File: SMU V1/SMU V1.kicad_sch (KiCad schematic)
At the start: 0 parts

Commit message: i forget what i changed
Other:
- sheet GPS ports: added GPS_LDO_EN; removed PP3300_GPS_VBCKUP
- sheet IMU ports: added IMU_INT1, IMU_INT2, IMU_SPI, PP5000_IMU_VSUPP; removed none
- sheet Main IO ports: added CAN, VBATT+; removed none
- sheet Microcontroller ports: added CAN, GPS_UART, IMU_SPI; removed none
- sheet Power ports: added PP3300_LDO_VOUT, PP5000_BUCK_VOUT, PPVAR_VBATT_RAW; removed none

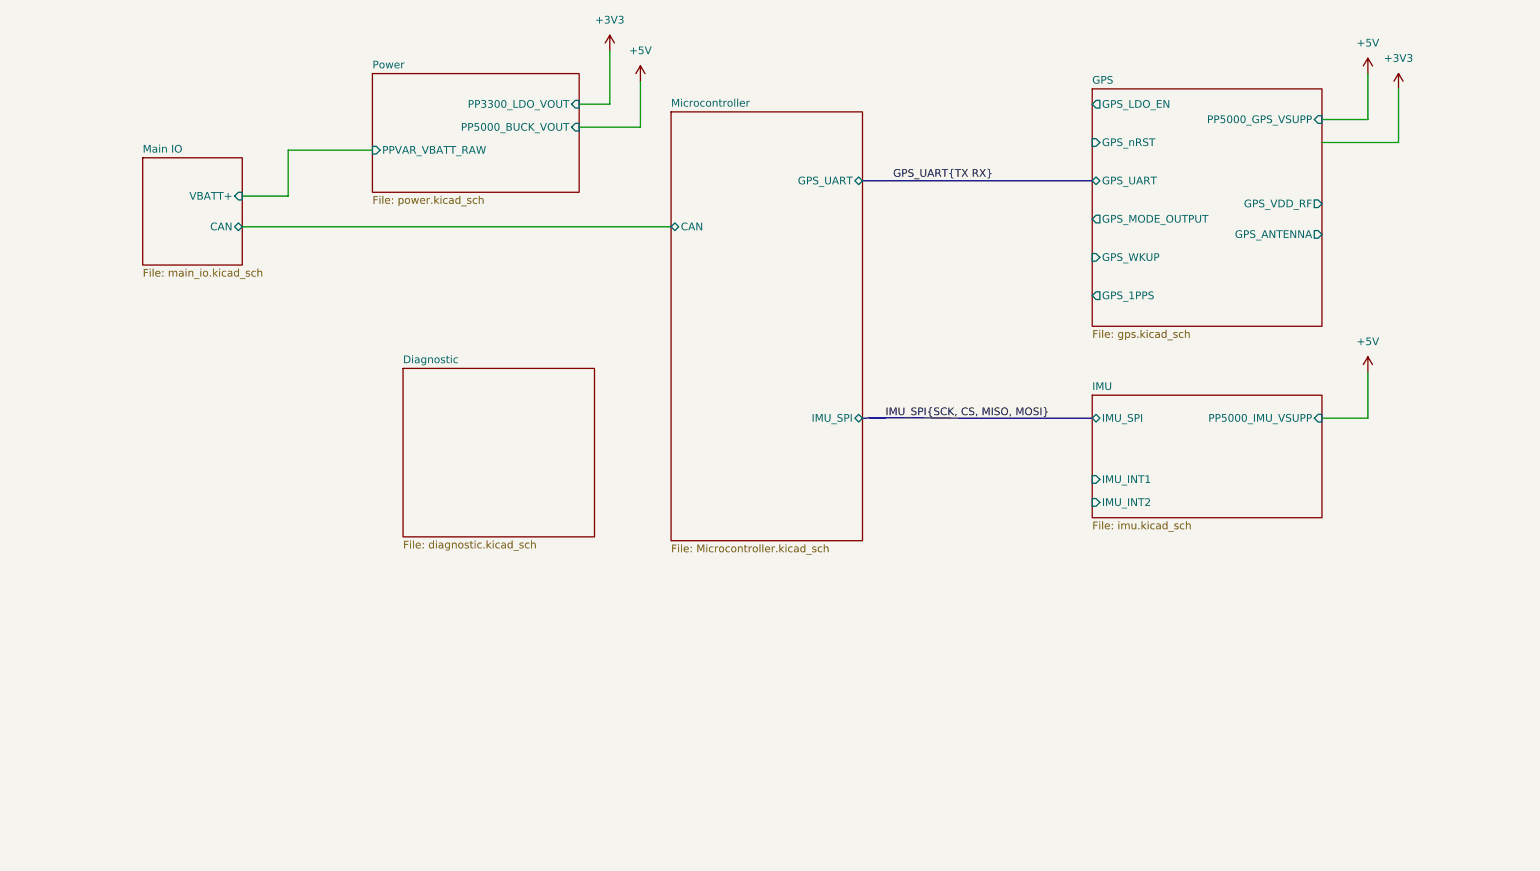
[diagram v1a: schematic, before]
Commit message: halfway done with routing, still needs antenna
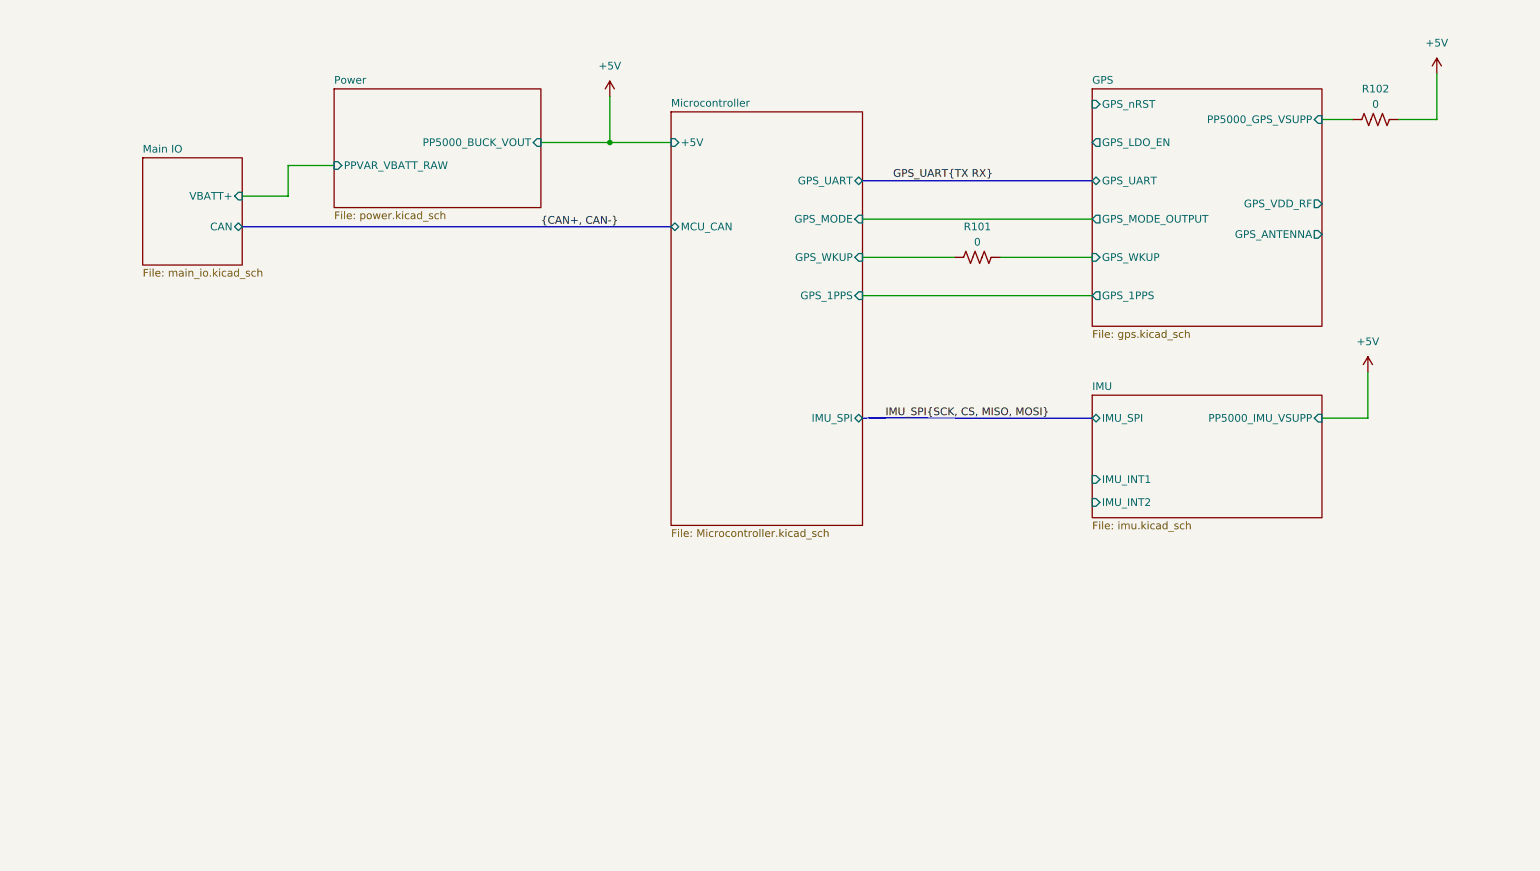
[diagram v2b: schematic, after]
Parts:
- added R101, R102: 0, Resistor_SMD:R_0603_1608Metric_Pad0.98x0.95mm_HandSolder, symbol bfr_resistors:RMCF0603ZT0R00
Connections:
- net +5V: now also R102.2
- net GPS/GPS_WKUP: now also R101.2
- new net GPS/PP5000_GPS_VSUPP: R102.1
- new net Microcontroller/GPS_WKUP: R101.1
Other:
- removed sheet Diagnostic
- sheet Microcontroller ports: added +5V, GPS_1PPS, GPS_MODE, GPS_WKUP, MCU_CAN; removed CAN
- sheet Power ports: added none; removed PP3300_LDO_VOUT

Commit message: finished, should prob double check the high frequency stuff
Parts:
- removed R101: 0, Resistor_SMD:R_0603_1608Metric_Pad0.98x0.95mm_HandSolder, symbol bfr_resistors:RMCF0603ZT0R00
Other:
- added sheet Antenna (antenna.kicad_sch)
- sheet GPS ports: added GPS_ANTENNA_RF, GPS_RF_VDD; removed GPS_ANTENNA, GPS_VDD_RF, GPS_WKUP
- sheet Microcontroller ports: added none; removed GPS_WKUP
- moved on the sheet: R102
